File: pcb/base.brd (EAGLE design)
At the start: 13.3 x 15.9 mm, 2 parts, among them IC1 27C64L

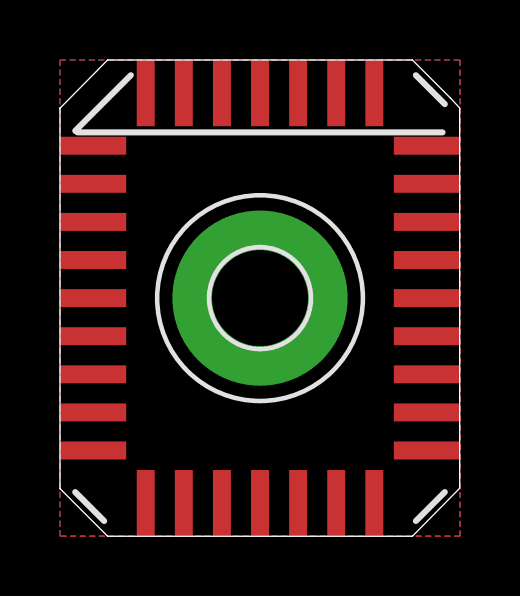
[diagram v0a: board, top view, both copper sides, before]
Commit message: Changed mounting pad for the cufflink back.
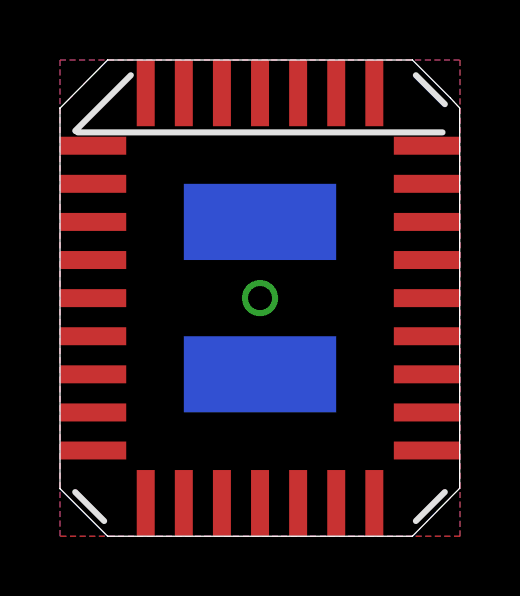
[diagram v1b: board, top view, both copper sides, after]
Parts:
- removed H1: MOUNT-PAD-ROUND3.2, holes:3,2-PAD
- added PAD1, PAD2: WIREPADSMD2,54-5,08, wirepad:SMD2,54-5,08
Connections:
- net GND: now also PAD1.1, PAD2.1; no longer H1.B3,2
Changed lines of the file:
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@@
 <attribute name="OC_NEWARK" value="unknown" x="6.6675" y="7.9375" size="1.778" layer="27" rot="R270" display="off"/>
 </element>
-<element name="H1" library="holes" package="3,2-PAD" value="MOUNT-PAD-ROUND3.2" x="6.6675" y="7.9375"/>
+<element name="PAD1" library="wirepad" package="SMD2,54-5,08" value="WIREPADSMD2,54-5,08" x="6.6675" y="5.3975" smashed="yes" rot="MR90"/>
+<element name="PAD2" library="wirepad" package="SMD2,54-5,08" value="WIREPADSMD2,54-5,08" x="6.6675" y="10.4775" smashed="yes" rot="MR270"/>
 </elements>
 <signals>
@@
 <vertex x="0" y="0"/>
 </polygon>
-<contactref element="H1" pad="B3,2"/>
+<contactref element="PAD1" pad="1"/>
+<contactref element="PAD2" pad="1"/>
+<via x="6.6675" y="7.9375" extent="1-16" drill="0.8" shape="square"/>
 <polygon width="0.4064" layer="16" isolate="0.4064">
 <vertex x="0" y="15.875"/>

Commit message: Connected the rest of the pins.
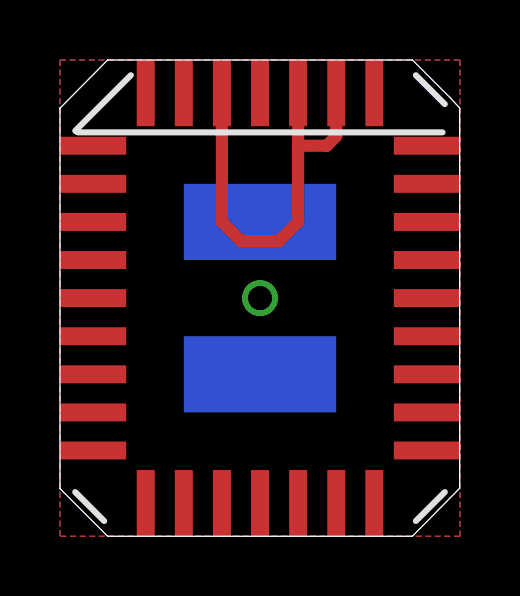
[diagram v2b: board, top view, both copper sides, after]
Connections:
- net GND: now also IC1.23, IC1.25
- net VCC: now also IC1.2, IC1.31
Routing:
- net VCC: track 0.00 -> 15.9 mm
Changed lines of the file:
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@@
 <layer number="27" name="tValues" color="7" fill="1" visible="yes" active="yes"/>
 <layer number="28" name="bValues" color="7" fill="1" visible="yes" active="yes"/>
-<layer number="29" name="tStop" color="7" fill="3" visible="no" active="yes"/>
-<layer number="30" name="bStop" color="7" fill="6" visible="no" active="yes"/>
-<layer number="31" name="tCream" color="7" fill="4" visible="no" active="yes"/>
-<layer number="32" name="bCream" color="7" fill="5" visible="no" active="yes"/>
-<layer number="33" name="tFinish" color="6" fill="3" visible="no" active="yes"/>
-<layer number="34" name="bFinish" color="6" fill="6" visible="no" active="yes"/>
-<layer number="35" name="tGlue" color="7" fill="4" visible="no" active="yes"/>
-<layer number="36" name="bGlue" color="7" fill="5" visible="no" active="yes"/>
-<layer number="37" name="tTest" color="7" fill="1" visible="no" active="yes"/>
-<layer number="38" name="bTest" color="7" fill="1" visible="no" active="yes"/>
+<layer number="29" name="tStop" color="7" fill="3" visible="yes" active="yes"/>
+<layer number="30" name="bStop" color="7" fill="6" visible="yes" active="yes"/>
+<layer number="31" name="tCream" color="7" fill="4" visible="yes" active="yes"/>
+<layer number="32" name="bCream" color="7" fill="5" visible="yes" active="yes"/>
+<layer number="33" name="tFinish" color="6" fill="3" visible="yes" active="yes"/>
+<layer number="34" name="bFinish" color="6" fill="6" visible="yes" active="yes"/>
+<layer number="35" name="tGlue" color="7" fill="4" visible="yes" active="yes"/>
+<layer number="36" name="bGlue" color="7" fill="5" visible="yes" active="yes"/>
+<layer number="37" name="tTest" color="7" fill="1" visible="yes" active="yes"/>
+<layer number="38" name="bTest" color="7" fill="1" visible="yes" active="yes"/>
 <layer number="39" name="tKeepout" color="4" fill="11" visible="yes" active="yes"/>
 <layer number="40" name="bKeepout" color="1" fill="11" visible="yes" active="yes"/>
@@
 <layer number="42" name="bRestrict" color="1" fill="10" visible="yes" active="yes"/>
 <layer number="43" name="vRestrict" color="2" fill="10" visible="yes" active="yes"/>
-<layer number="44" name="Drills" color="7" fill="1" visible="no" active="yes"/>
+<layer number="44" name="Drills" color="7" fill="1" visible="yes" active="yes"/>
 <layer number="45" name="Holes" color="7" fill="1" visible="yes" active="yes"/>
-<layer number="46" name="Milling" color="3" fill="1" visible="no" active="yes"/>
-<layer number="47" name="Measures" color="7" fill="1" visible="no" active="yes"/>
+<layer number="46" name="Milling" color="3" fill="1" visible="yes" active="yes"/>
+<layer number="47" name="Measures" color="7" fill="1" visible="yes" active="yes"/>
 <layer number="48" name="Document" color="7" fill="1" visible="yes" active="yes"/>
 <layer number="49" name="Reference" color="7" fill="1" visible="yes" active="yes"/>
@@
 </elements>
 <signals>
-<signal name="VCC">
-<contactref element="IC1" pad="32"/>
-</signal>
 <signal name="GND">
 <contactref element="IC1" pad="16"/>
@@
 <vertex x="0" y="0"/>
 </polygon>
+<contactref element="IC1" pad="25"/>
+<contactref element="IC1" pad="23"/>
+</signal>
+<signal name="VCC">
+<contactref element="IC1" pad="32"/>
+<contactref element="IC1" pad="2"/>
+<wire x1="5.3975" y1="14.7675" x2="5.3975" y2="13.335" width="0.4064" layer="1"/>
+<wire x1="5.3975" y1="14.7675" x2="5.3975" y2="10.4775" width="0.4064" layer="1"/>
+<wire x1="5.3975" y1="10.4775" x2="6.0325" y2="9.8425" width="0.4064" layer="1"/>
+<wire x1="6.0325" y1="9.8425" x2="7.3025" y2="9.8425" width="0.4064" layer="1"/>
+<wire x1="7.3025" y1="9.8425" x2="7.9375" y2="10.4775" width="0.4064" layer="1"/>
+<wire x1="7.9375" y1="10.4775" x2="7.9375" y2="13.0175" width="0.4064" layer="1"/>
+<contactref element="IC1" pad="31"/>
+<wire x1="7.9375" y1="13.0175" x2="7.9375" y2="14.7675" width="0.4064" layer="1"/>
+<wire x1="9.2075" y1="14.7675" x2="9.2075" y2="13.335" width="0.4064" layer="1"/>
+<wire x1="9.2075" y1="13.335" x2="8.89" y2="13.0175" width="0.4064" layer="1"/>
+<wire x1="8.89" y1="13.0175" x2="7.9375" y2="13.0175" width="0.4064" layer="1"/>
 </signal>
 </signals>
